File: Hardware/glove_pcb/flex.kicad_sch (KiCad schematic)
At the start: 15 parts, among them J19 Potentiometers

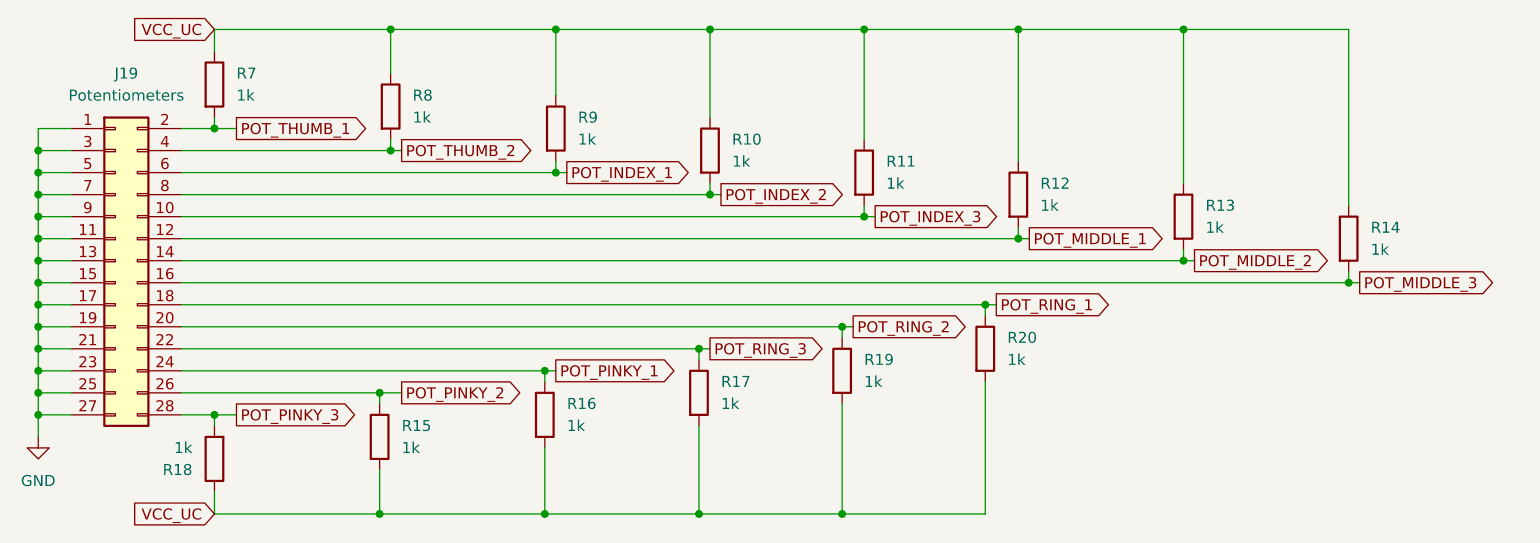
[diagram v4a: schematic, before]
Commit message: Add titles to pages and reannotate
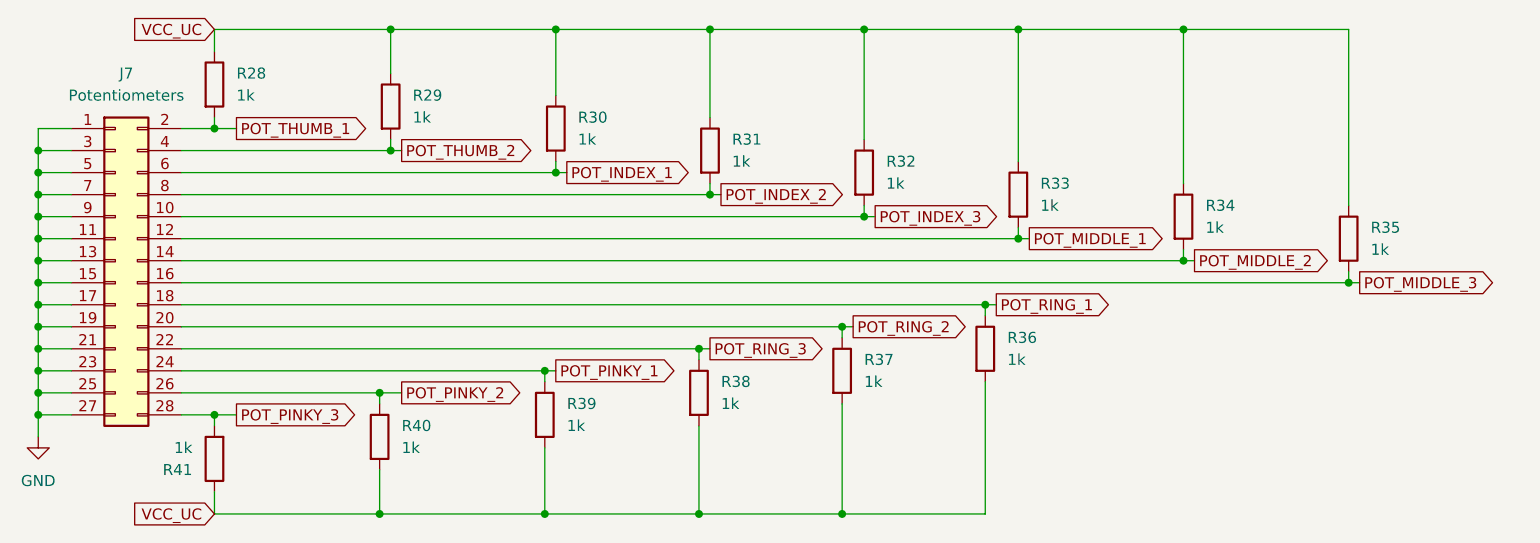
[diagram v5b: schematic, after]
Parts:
- renumbered J19 to J7, R7 to R28, R8 to R29, R9 to R30, R10 to R31, R11 to R32, R12 to R33, R13 to R34, R14 to R35, R20 to R36, R19 to R37, R17 to R38, R16 to R39, R15 to R40, R18 to R41
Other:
- company: (none) -> COEN 490 Team 15
- title: (none) -> Flex Potentiometer Connections
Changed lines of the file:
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@@
 (kicad_sch (version 20230121) (generator eeschema)
   (paper "USLetter")
+  (title_block
+    (title "Flex Potentiometer Connections")
+    (date "2023-11-24")
+    (company "COEN 490 Team 15")
+  )
   (junction (at 53.34 90.17) (diameter 0) (color 0 0 0 0)
   )
@@
   (symbol (lib_id "Device:R") (at 162.56 90.17 0) (unit 1)
     (in_bom yes) (on_board yes) (dnp no) (fields_autoplaced)
-    (property "Reference" "R20" (at 165.1 88.9 0)
+    (property "Reference" "R36" (at 165.1 88.9 0)
       (effects (font (size 1.27 1.27)) (justify left))
     )
@@
       (project "glove_pcb"
         (path "/747ff5f3-d342-40b0-8e4e-75b3a3063e75/bbbc9975-a050-48bd-8c18-11f2eff17087"
-          (reference "R20") (unit 1)
+          (reference "R36") (unit 1)
         )
       )
@@
   (symbol (lib_id "Device:R") (at 166.37 72.39 0) (unit 1)
     (in_bom yes) (on_board yes) (dnp no) (fields_autoplaced)
-    (property "Reference" "R12" (at 168.91 71.12 0)
+    (property "Reference" "R33" (at 168.91 71.12 0)
       (effects (font (size 1.27 1.27)) (justify left))
     )
@@
       (project "glove_pcb"
         (path "/747ff5f3-d342-40b0-8e4e-75b3a3063e75/bbbc9975-a050-48bd-8c18-11f2eff17087"
-          (reference "R12") (unit 1)
+          (reference "R33") (unit 1)
         )
       )
@@
   (symbol (lib_id "Device:R") (at 146.05 92.71 0) (unit 1)
     (in_bom yes) (on_board yes) (dnp no) (fields_autoplaced)
-    (property "Reference" "R19" (at 148.59 91.44 0)
+    (property "Reference" "R37" (at 148.59 91.44 0)
       (effects (font (size 1.27 1.27)) (justify left))
     )
@@
       (project "glove_pcb"
         (path "/747ff5f3-d342-40b0-8e4e-75b3a3063e75/bbbc9975-a050-48bd-8c18-11f2eff17087"
-          (reference "R19") (unit 1)
+          (reference "R37") (unit 1)
         )
       )
@@
   (symbol (lib_id "Device:R") (at 185.42 74.93 0) (unit 1)
     (in_bom yes) (on_board yes) (dnp no) (fields_autoplaced)
-    (property "Reference" "R13" (at 187.96 73.66 0)
+    (property "Reference" "R34" (at 187.96 73.66 0)
       (effects (font (size 1.27 1.27)) (justify left))
     )
@@
       (project "glove_pcb"
         (path "/747ff5f3-d342-40b0-8e4e-75b3a3063e75/bbbc9975-a050-48bd-8c18-11f2eff17087"
-          (reference "R13") (unit 1)
+          (reference "R34") (unit 1)
         )
       )
@@
   (symbol (lib_id "Device:R") (at 130.81 67.31 0) (unit 1)
     (in_bom yes) (on_board yes) (dnp no) (fields_autoplaced)
-    (property "Reference" "R10" (at 133.35 66.04 0)
+    (property "Reference" "R31" (at 133.35 66.04 0)
       (effects (font (size 1.27 1.27)) (justify left))
     )
@@
       (project "glove_pcb"
         (path "/747ff5f3-d342-40b0-8e4e-75b3a3063e75/bbbc9975-a050-48bd-8c18-11f2eff17087"
-          (reference "R10") (unit 1)
+          (reference "R31") (unit 1)
         )
       )
@@
   (symbol (lib_id "Device:R") (at 92.71 100.33 0) (unit 1)
     (in_bom yes) (on_board yes) (dnp no) (fields_autoplaced)
-    (property "Reference" "R15" (at 95.25 99.06 0)
+    (property "Reference" "R40" (at 95.25 99.06 0)
       (effects (font (size 1.27 1.27)) (justify left))
     )
@@
       (project "glove_pcb"
         (path "/747ff5f3-d342-40b0-8e4e-75b3a3063e75/bbbc9975-a050-48bd-8c18-11f2eff17087"
-          (reference "R15") (unit 1)
+          (reference "R40") (unit 1)
         )
       )
@@
   (symbol (lib_id "Connector_Generic:Conn_02x14_Odd_Even") (at 62.23 80.01 0) (unit 1)
     (in_bom yes) (on_board yes) (dnp no) (fields_autoplaced)
-    (property "Reference" "J19" (at 63.5 58.42 0)
+    (property "Reference" "J7" (at 63.5 58.42 0)
       (effects (font (size 1.27 1.27)))
     )
@@
       (project "glove_pcb"
         (path "/747ff5f3-d342-40b0-8e4e-75b3a3063e75/bbbc9975-a050-48bd-8c18-11f2eff17087"
-          (reference "J19") (unit 1)
+          (reference "J7") (unit 1)
         )
       )
@@
   (symbol (lib_id "Device:R") (at 204.47 77.47 0) (unit 1)
     (in_bom yes) (on_board yes) (dnp no) (fields_autoplaced)
-    (property "Reference" "R14" (at 207.01 76.2 0)
+    (property "Reference" "R35" (at 207.01 76.2 0)
       (effects (font (size 1.27 1.27)) (justify left))
     )
@@
       (project "glove_pcb"
         (path "/747ff5f3-d342-40b0-8e4e-75b3a3063e75/bbbc9975-a050-48bd-8c18-11f2eff17087"
-          (reference "R14") (unit 1)
+          (reference "R35") (unit 1)
         )
       )
@@
   (symbol (lib_id "Device:R") (at 129.54 95.25 0) (unit 1)
     (in_bom yes) (on_board yes) (dnp no) (fields_autoplaced)
-    (property "Reference" "R17" (at 132.08 93.98 0)
+    (property "Reference" "R38" (at 132.08 93.98 0)
       (effects (font (size 1.27 1.27)) (justify left))
     )
@@
       (project "glove_pcb"
         (path "/747ff5f3-d342-40b0-8e4e-75b3a3063e75/bbbc9975-a050-48bd-8c18-11f2eff17087"
-          (reference "R17") (unit 1)
+          (reference "R38") (unit 1)
         )
       )
@@
   (symbol (lib_id "Device:R") (at 73.66 102.87 180) (unit 1)
     (in_bom yes) (on_board yes) (dnp no) (fields_autoplaced)
-    (property "Reference" "R18" (at 71.12 104.14 0)
+    (property "Reference" "R41" (at 71.12 104.14 0)
       (effects (font (size 1.27 1.27)) (justify left))
     )
@@
       (project "glove_pcb"
         (path "/747ff5f3-d342-40b0-8e4e-75b3a3063e75/bbbc9975-a050-48bd-8c18-11f2eff17087"
-          (reference "R18") (unit 1)
+          (reference "R41") (unit 1)
         )
       )
@@
   (symbol (lib_id "power:GND") (at 53.34 100.33 0) (unit 1)
     (in_bom yes) (on_board yes) (dnp no) (fields_autoplaced)
-    (property "Reference" "#PWR05" (at 53.34 106.68 0)
+    (property "Reference" "#PWR045" (at 53.34 106.68 0)
       (effects (font (size 1.27 1.27)) hide)
     )
@@
       (project "glove_pcb"
         (path "/747ff5f3-d342-40b0-8e4e-75b3a3063e75/bbbc9975-a050-48bd-8c18-11f2eff17087"
-          (reference "#PWR05") (unit 1)
+          (reference "#PWR045") (unit 1)
         )
       )
@@
   (symbol (lib_id "Device:R") (at 111.76 97.79 0) (unit 1)
     (in_bom yes) (on_board yes) (dnp no) (fields_autoplaced)
-    (property "Reference" "R16" (at 114.3 96.52 0)
+    (property "Reference" "R39" (at 114.3 96.52 0)
       (effects (font (size 1.27 1.27)) (justify left))
     )
@@
       (project "glove_pcb"
         (path "/747ff5f3-d342-40b0-8e4e-75b3a3063e75/bbbc9975-a050-48bd-8c18-11f2eff17087"
-          (reference "R16") (unit 1)
+          (reference "R39") (unit 1)
         )
       )
@@
   (symbol (lib_id "Device:R") (at 73.66 59.69 0) (unit 1)
     (in_bom yes) (on_board yes) (dnp no) (fields_autoplaced)
-    (property "Reference" "R7" (at 76.2 58.42 0)
+    (property "Reference" "R28" (at 76.2 58.42 0)
       (effects (font (size 1.27 1.27)) (justify left))
     )
@@
       (project "glove_pcb"
         (path "/747ff5f3-d342-40b0-8e4e-75b3a3063e75/bbbc9975-a050-48bd-8c18-11f2eff17087"
-          (reference "R7") (unit 1)
+          (reference "R28") (unit 1)
         )
       )
@@
   (symbol (lib_id "Device:R") (at 148.59 69.85 0) (unit 1)
     (in_bom yes) (on_board yes) (dnp no) (fields_autoplaced)
-    (property "Reference" "R11" (at 151.13 68.58 0)
+    (property "Reference" "R32" (at 151.13 68.58 0)
       (effects (font (size 1.27 1.27)) (justify left))
     )
@@
       (project "glove_pcb"
         (path "/747ff5f3-d342-40b0-8e4e-75b3a3063e75/bbbc9975-a050-48bd-8c18-11f2eff17087"
-          (reference "R11") (unit 1)
+          (reference "R32") (unit 1)
         )
       )
@@
   (symbol (lib_id "Device:R") (at 113.03 64.77 0) (unit 1)
     (in_bom yes) (on_board yes) (dnp no) (fields_autoplaced)
-    (property "Reference" "R9" (at 115.57 63.5 0)
+    (property "Reference" "R30" (at 115.57 63.5 0)
       (effects (font (size 1.27 1.27)) (justify left))
     )
@@
       (project "glove_pcb"
         (path "/747ff5f3-d342-40b0-8e4e-75b3a3063e75/bbbc9975-a050-48bd-8c18-11f2eff17087"
-          (reference "R9") (unit 1)
+          (reference "R30") (unit 1)
         )
       )
@@
   (symbol (lib_id "Device:R") (at 93.98 62.23 0) (unit 1)
     (in_bom yes) (on_board yes) (dnp no) (fields_autoplaced)
-    (property "Reference" "R8" (at 96.52 60.96 0)
+    (property "Reference" "R29" (at 96.52 60.96 0)
       (effects (font (size 1.27 1.27)) (justify left))
     )
@@
       (project "glove_pcb"
         (path "/747ff5f3-d342-40b0-8e4e-75b3a3063e75/bbbc9975-a050-48bd-8c18-11f2eff17087"
-          (reference "R8") (unit 1)
-        )
-      )
+          (reference "R29") (unit 1)
+        )
+      )

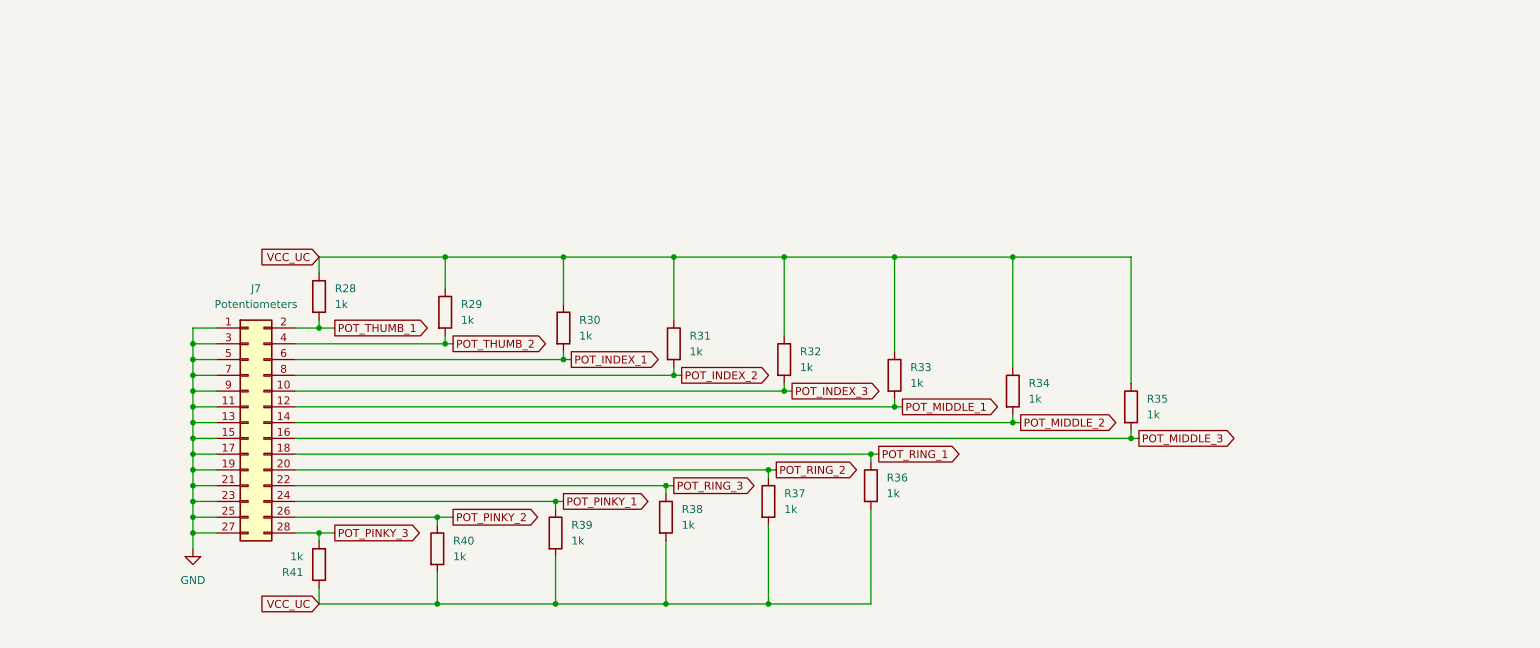
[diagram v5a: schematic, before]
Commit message: Finalize schematic for real this time
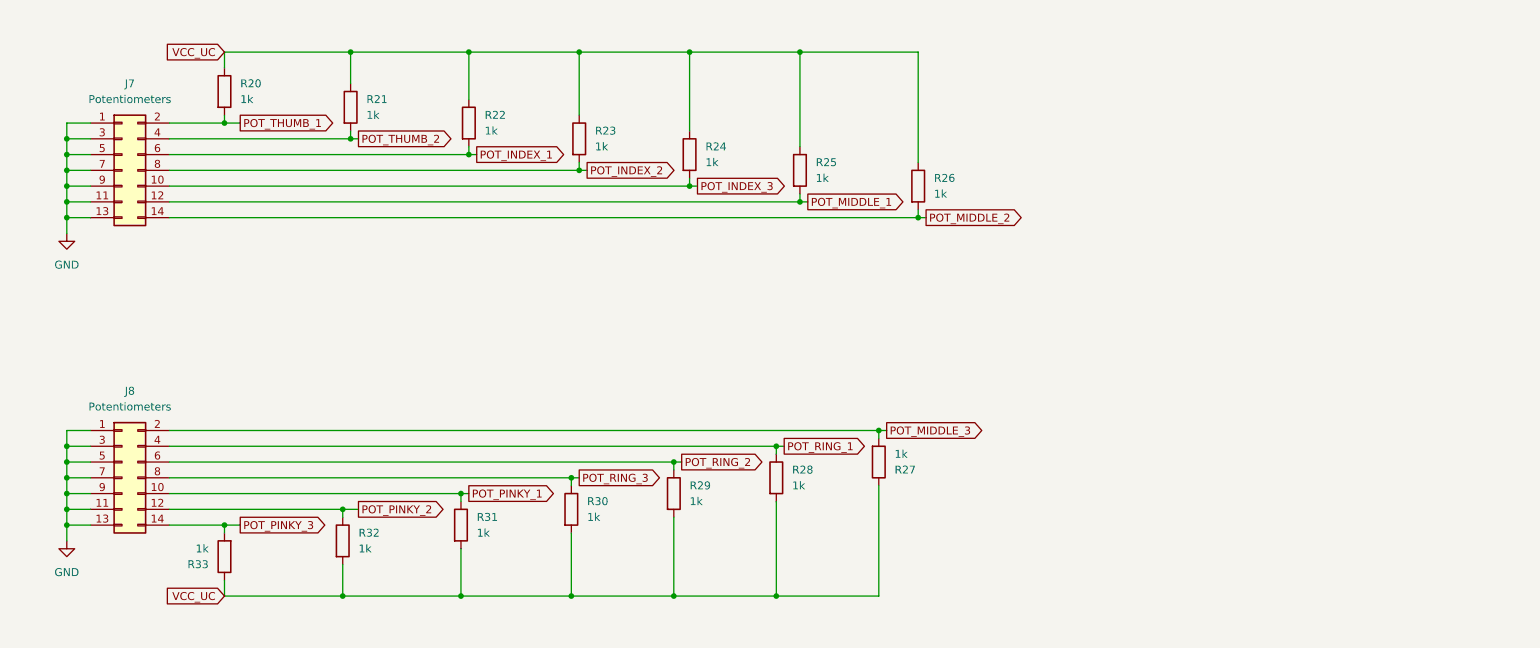
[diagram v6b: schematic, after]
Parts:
- removed J7: Potentiometers, symbol Connector_Generic:Conn_02x14_Odd_Even
- added J7, J8: Potentiometers, symbol Connector_Generic:Conn_02x07_Odd_Even
- renumbered R28 to R20, R29 to R21, R30 to R22, R31 to R23, R32 to R24, R33 to R25, R34 to R26, R35 to R27, R36 to R28, R37 to R29, R38 to R30, R39 to R31, R40 to R32, R41 to R33
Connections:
- net GND: now also J7.1 (Pin_1), J7.11 (Pin_11), J7.13 (Pin_13), J7.3 (Pin_3), J7.5 (Pin_5), J7.7 (Pin_7), J7.9 (Pin_9), J8.1 (Pin_1), J8.11 (Pin_11), J8.13 (Pin_13), J8.3 (Pin_3), J8.5 (Pin_5), J8.7 (Pin_7), J8.9 (Pin_9)
- net POT_INDEX_1: now also J7.6 (Pin_6)
- net POT_INDEX_2: now also J7.8 (Pin_8)
- net POT_INDEX_3: now also J7.10 (Pin_10)
- net POT_MIDDLE_1: now also J7.12 (Pin_12)
- net POT_MIDDLE_2: now also J7.14 (Pin_14)
- net POT_MIDDLE_3: now also J8.2 (Pin_2)
- net POT_PINKY_1: now also J8.10 (Pin_10)
- net POT_PINKY_2: now also J8.12 (Pin_12)
- net POT_PINKY_3: now also J8.14 (Pin_14)
- net POT_RING_1: now also J8.4 (Pin_4)
- net POT_RING_2: now also J8.6 (Pin_6)
- net POT_RING_3: now also J8.8 (Pin_8)
- net POT_THUMB_1: now also J7.2 (Pin_2)
- net POT_THUMB_2: now also J7.4 (Pin_4)
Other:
- moved on the sheet: R20, R21, R22, R23, R24, R25, R26, R27, R28, R29, R30, R31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

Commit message: Added Footprints
I Added footprints for every components in PCB
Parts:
- J7, J8: footprint (none) -> Connector_PinSocket_2.54mm:PinSocket_2x07_P2.54mm_Vertical
- R20, R21, R22, R23, R24, R25, R26, R27, R28, R29, R30, R31, R32, R33: footprint (none) -> Resistor_SMD:R_0805_2012Metric_Pad1.20x1.40mm_HandSolder
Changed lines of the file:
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@@
       (effects (font (size 1.27 1.27)) (justify left))
     )
-    (property "Footprint" "" (at 145.542 88.9 90)
+    (property "Footprint" "Resistor_SMD:R_0805_2012Metric_Pad1.20x1.40mm_HandSolder" (at 145.542 88.9 90)
       (effects (font (size 1.27 1.27)) hide)
     )
@@
       (effects (font (size 1.27 1.27)) (justify left))
     )
-    (property "Footprint" "" (at 149.352 39.37 90)
+    (property "Footprint" "Resistor_SMD:R_0805_2012Metric_Pad1.20x1.40mm_HandSolder" (at 149.352 39.37 90)
       (effects (font (size 1.27 1.27)) hide)
     )
@@
       (effects (font (size 1.27 1.27)) (justify left))
     )
-    (property "Footprint" "" (at 129.032 91.44 90)
+    (property "Footprint" "Resistor_SMD:R_0805_2012Metric_Pad1.20x1.40mm_HandSolder" (at 129.032 91.44 90)
       (effects (font (size 1.27 1.27)) hide)
     )
@@
       (effects (font (size 1.27 1.27)) (justify left))
     )
-    (property "Footprint" "" (at 168.402 41.91 90)
+    (property "Footprint" "Resistor_SMD:R_0805_2012Metric_Pad1.20x1.40mm_HandSolder" (at 168.402 41.91 90)
       (effects (font (size 1.27 1.27)) hide)
     )
@@
       (effects (font (size 1.27 1.27)))
     )
-    (property "Footprint" "" (at 41.91 39.37 0)
+    (property "Footprint" "Connector_PinSocket_2.54mm:PinSocket_2x07_P2.54mm_Vertical" (at 41.91 39.37 0)
       (effects (font (size 1.27 1.27)) hide)
     )
@@
       (effects (font (size 1.27 1.27)) (justify left))
     )
-    (property "Footprint" "" (at 113.792 34.29 90)
+    (property "Footprint" "Resistor_SMD:R_0805_2012Metric_Pad1.20x1.40mm_HandSolder" (at 113.792 34.29 90)
       (effects (font (size 1.27 1.27)) hide)
     )
@@
       (effects (font (size 1.27 1.27)) (justify left))
     )
-    (property "Footprint" "" (at 75.692 99.06 90)
+    (property "Footprint" "Resistor_SMD:R_0805_2012Metric_Pad1.20x1.40mm_HandSolder" (at 75.692 99.06 90)
       (effects (font (size 1.27 1.27)) hide)
     )
@@
       (effects (font (size 1.27 1.27)) (justify left))
     )
-    (property "Footprint" "" (at 162.052 86.36 90)
+    (property "Footprint" "Resistor_SMD:R_0805_2012Metric_Pad1.20x1.40mm_HandSolder" (at 162.052 86.36 90)
       (effects (font (size 1.27 1.27)) hide)
     )
@@
       (effects (font (size 1.27 1.27)) (justify left))
     )
-    (property "Footprint" "" (at 112.522 93.98 90)
+    (property "Footprint" "Resistor_SMD:R_0805_2012Metric_Pad1.20x1.40mm_HandSolder" (at 112.522 93.98 90)
       (effects (font (size 1.27 1.27)) hide)
     )
@@
       (effects (font (size 1.27 1.27)) (justify left))
     )
-    (property "Footprint" "" (at 60.198 101.6 90)
+    (property "Footprint" "Resistor_SMD:R_0805_2012Metric_Pad1.20x1.40mm_HandSolder" (at 60.198 101.6 90)
       (effects (font (size 1.27 1.27)) hide)
     )
@@
       (effects (font (size 1.27 1.27)) (justify left))
     )
-    (property "Footprint" "" (at 94.742 96.52 90)
+    (property "Footprint" "Resistor_SMD:R_0805_2012Metric_Pad1.20x1.40mm_HandSolder" (at 94.742 96.52 90)
       (effects (font (size 1.27 1.27)) hide)
     )
@@
       (effects (font (size 1.27 1.27)))
     )
-    (property "Footprint" "" (at 41.91 88.9 0)
+    (property "Footprint" "Connector_PinSocket_2.54mm:PinSocket_2x07_P2.54mm_Vertical" (at 41.91 88.9 0)
       (effects (font (size 1.27 1.27)) hide)
     )
@@
       (effects (font (size 1.27 1.27)) (justify left))
     )
-    (property "Footprint" "" (at 56.642 26.67 90)
+    (property "Footprint" "Resistor_SMD:R_0805_2012Metric_Pad1.20x1.40mm_HandSolder" (at 56.642 26.67 90)
       (effects (font (size 1.27 1.27)) hide)
     )
@@
       (effects (font (size 1.27 1.27)) (justify left))
     )
-    (property "Footprint" "" (at 131.572 36.83 90)
+    (property "Footprint" "Resistor_SMD:R_0805_2012Metric_Pad1.20x1.40mm_HandSolder" (at 131.572 36.83 90)
       (effects (font (size 1.27 1.27)) hide)
     )
@@
       (effects (font (size 1.27 1.27)) (justify left))
     )
-    (property "Footprint" "" (at 96.012 31.75 90)
+    (property "Footprint" "Resistor_SMD:R_0805_2012Metric_Pad1.20x1.40mm_HandSolder" (at 96.012 31.75 90)
       (effects (font (size 1.27 1.27)) hide)
     )
@@
       (effects (font (size 1.27 1.27)) (justify left))
     )
-    (property "Footprint" "" (at 76.962 29.21 90)
-      (effects (font (size 1.27 1.27)) hide)
-    )
+    (property "Footprint" "Resistor_SMD:R_0805_2012Metric_Pad1.20x1.40mm_HandSolder" (at 76.962 29.21 90)
+      (effects (font (size 1.27 1.27)) hide)
+    )
